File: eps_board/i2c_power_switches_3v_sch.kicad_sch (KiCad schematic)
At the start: 10 parts, among them U34 MCP23017T-E/SS

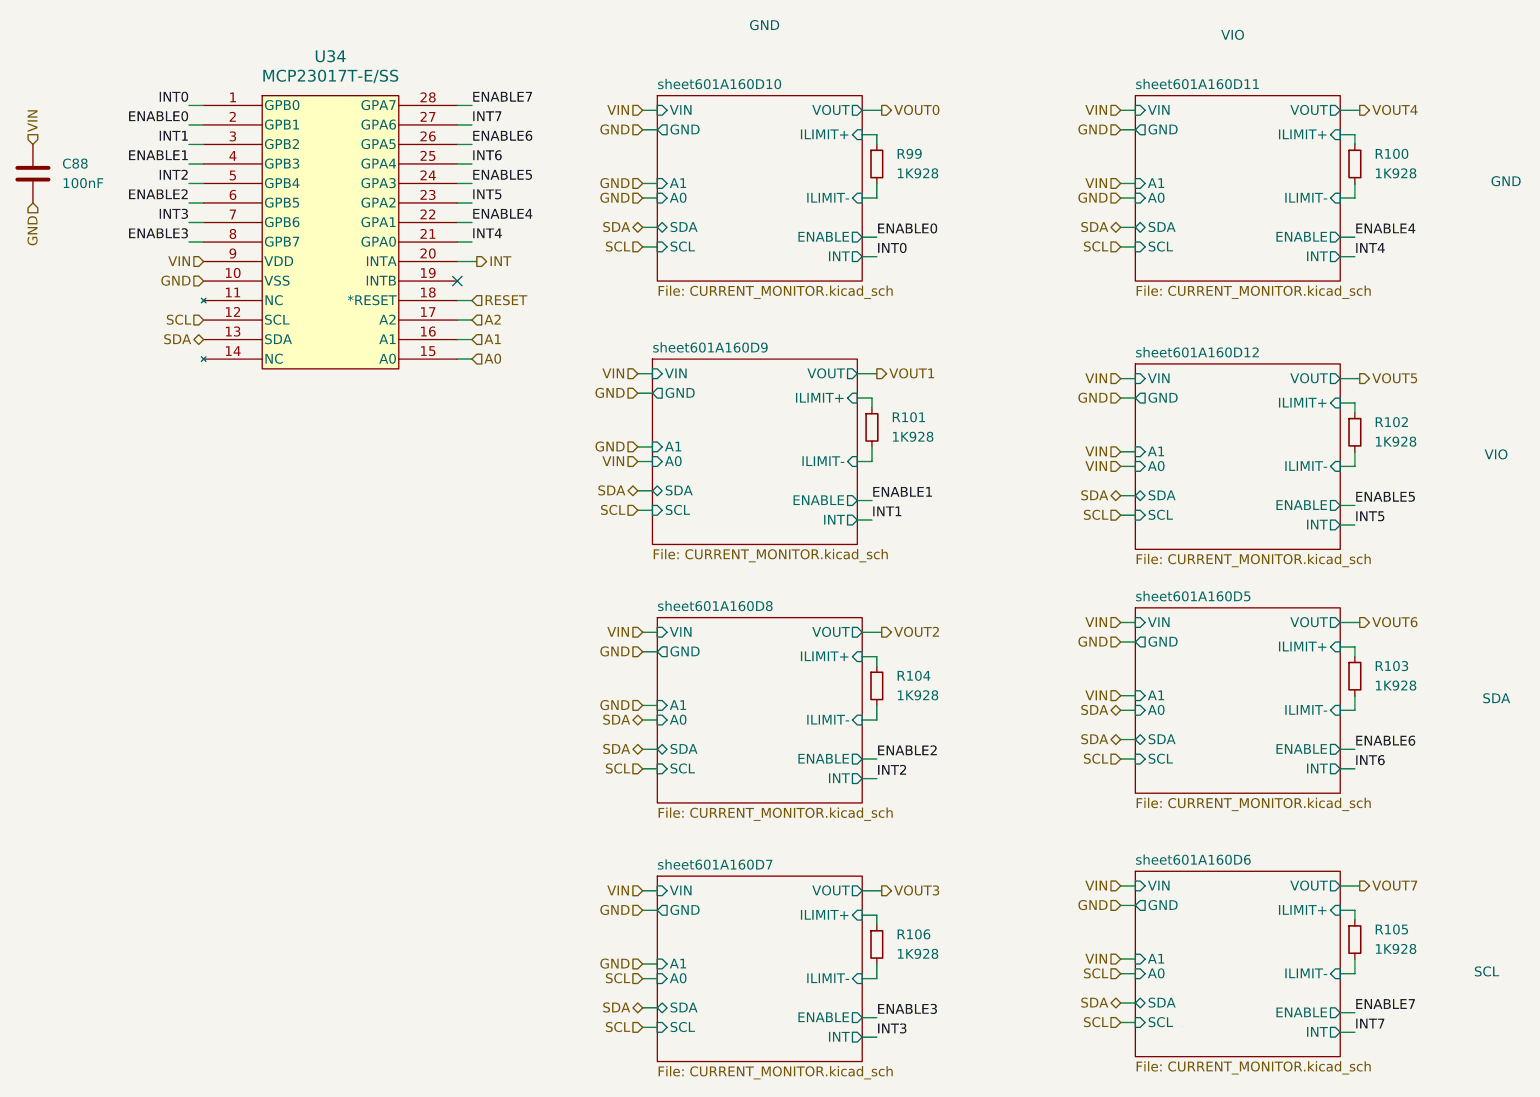
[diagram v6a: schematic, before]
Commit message: use small connectors in corners and on sides for sun sensors and solar cells
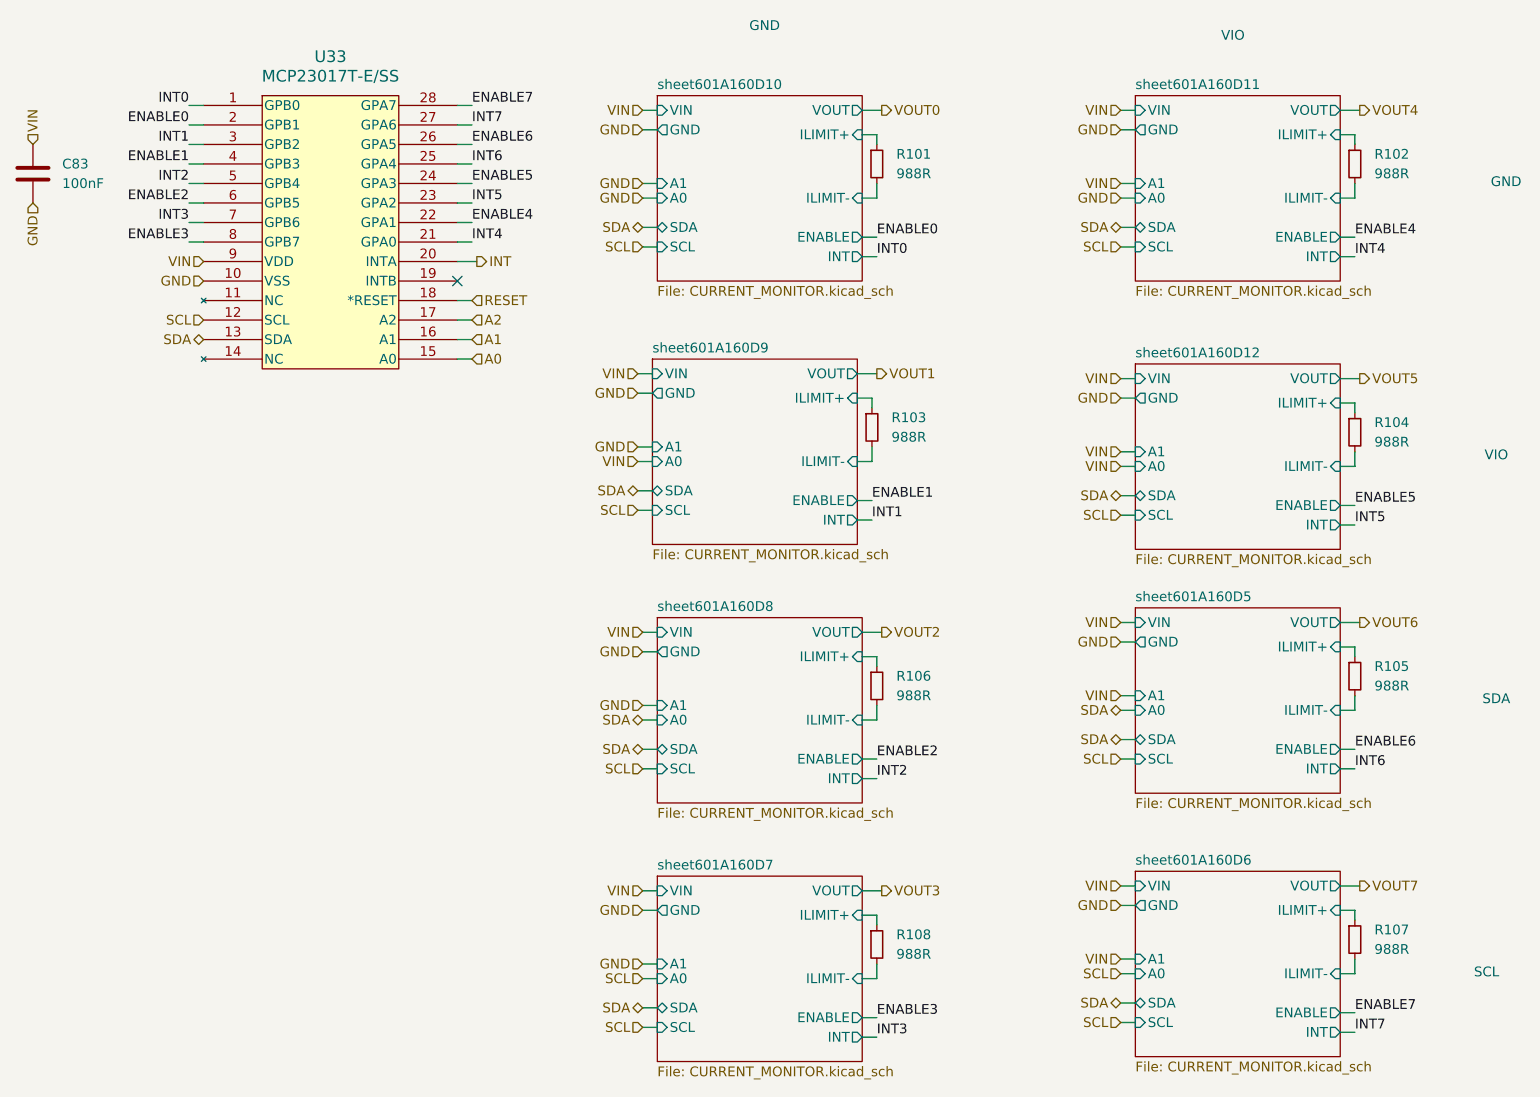
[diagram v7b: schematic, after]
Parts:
- R101: renamed from R99; value 1K928 -> 988R; Part Number RC0603FR-071K928L -> RT0603DRE07988RL; Tolerance 1 -> 0.5
- R102: renamed from R100; value 1K928 -> 988R; Part Number RC0603FR-071K928L -> RT0603DRE07988RL; Tolerance 1 -> 0.5
- R103: renamed from R101; value 1K928 -> 988R; Part Number RC0603FR-071K928L -> RT0603DRE07988RL; Tolerance 1 -> 0.5
- R104: renamed from R102; value 1K928 -> 988R; Part Number RC0603FR-071K928L -> RT0603DRE07988RL; Tolerance 1 -> 0.5
- R105: renamed from R103; value 1K928 -> 988R; Part Number RC0603FR-071K928L -> RT0603DRE07988RL; Tolerance 1 -> 0.5
- R106: renamed from R104; value 1K928 -> 988R; Part Number RC0603FR-071K928L -> RT0603DRE07988RL; Tolerance 1 -> 0.5
- R107: renamed from R105; value 1K928 -> 988R; Part Number RC0603FR-071K928L -> RT0603DRE07988RL; Tolerance 1 -> 0.5
- R108: renamed from R106; value 1K928 -> 988R; Part Number RC0603FR-071K928L -> RT0603DRE07988RL; Tolerance 1 -> 0.5
- renumbered C88 to C83, U34 to U33

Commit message: detailed power switches moved from EPS to invidual boards, each board only has core and aux bus (and batt if needed) which scales better. Reassign PC104 slots
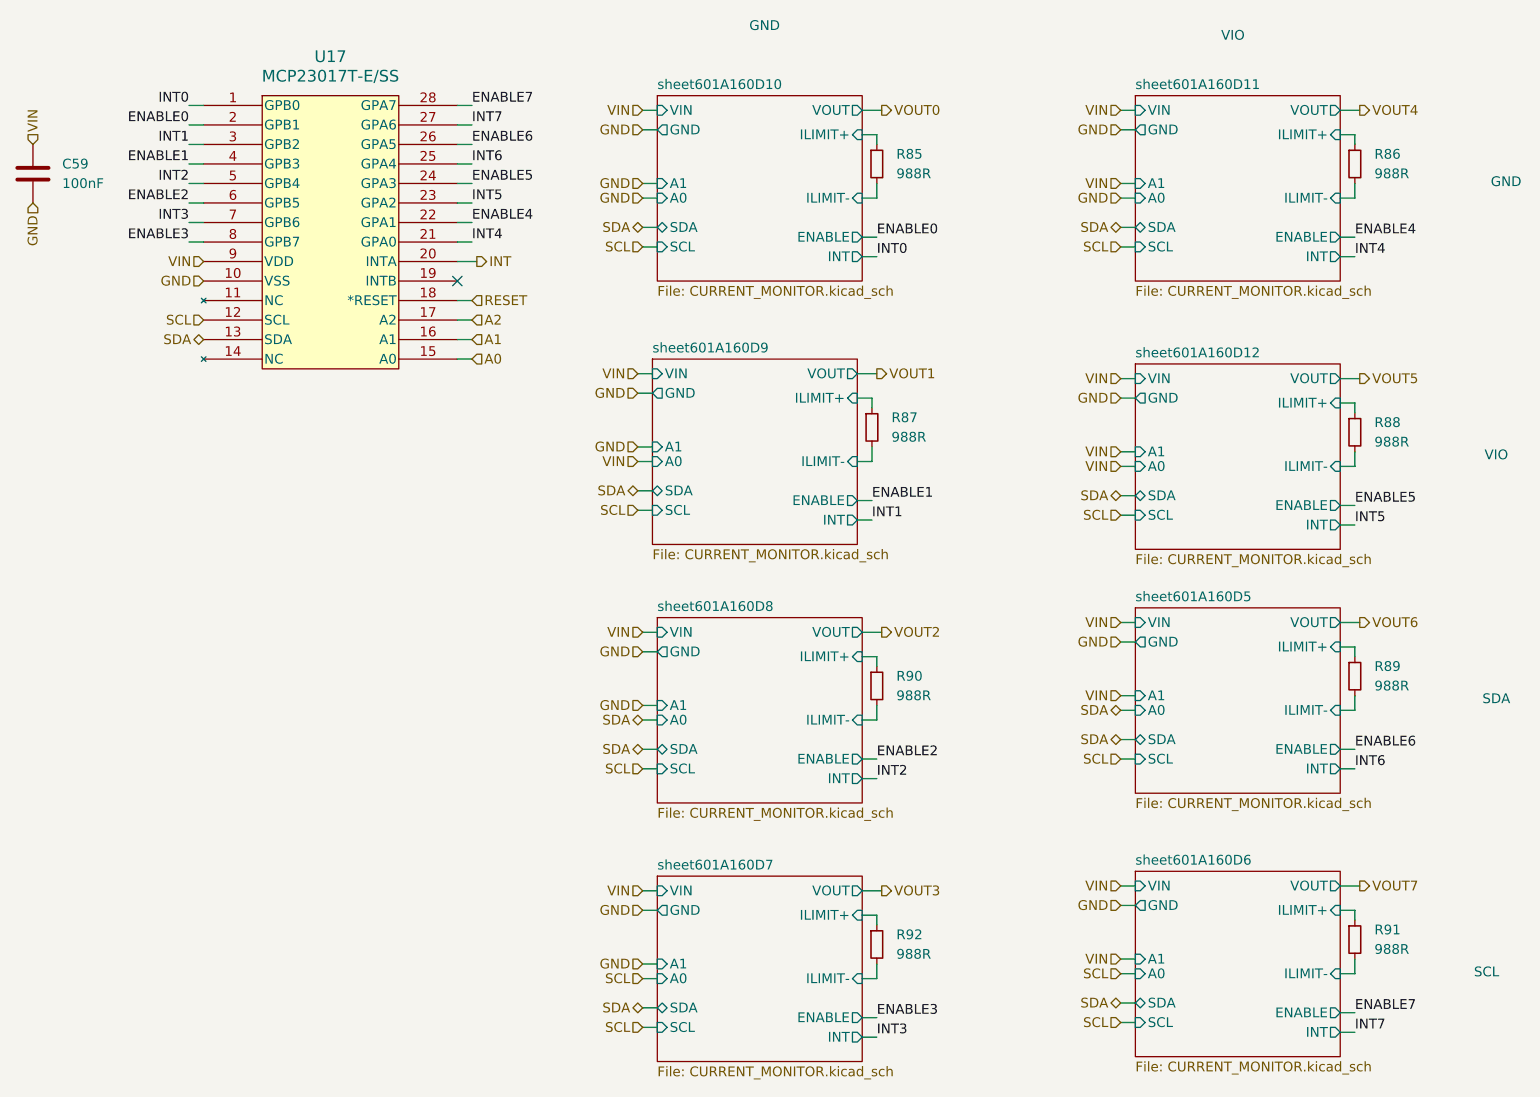
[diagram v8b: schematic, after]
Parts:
- renumbered C83 to C59, R101 to R85, R102 to R86, R103 to R87, R104 to R88, R105 to R89, R106 to R90, R107 to R91, R108 to R92, U33 to U17
